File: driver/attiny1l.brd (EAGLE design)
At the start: 160 x 100 mm, 7 parts, among them IC1 ATTiny85, IC2 74AHC1G00DCK, IC3 74AHC1G00DCK, IC4 LB1973M, J1 AVR_SPI_PRG_6NS

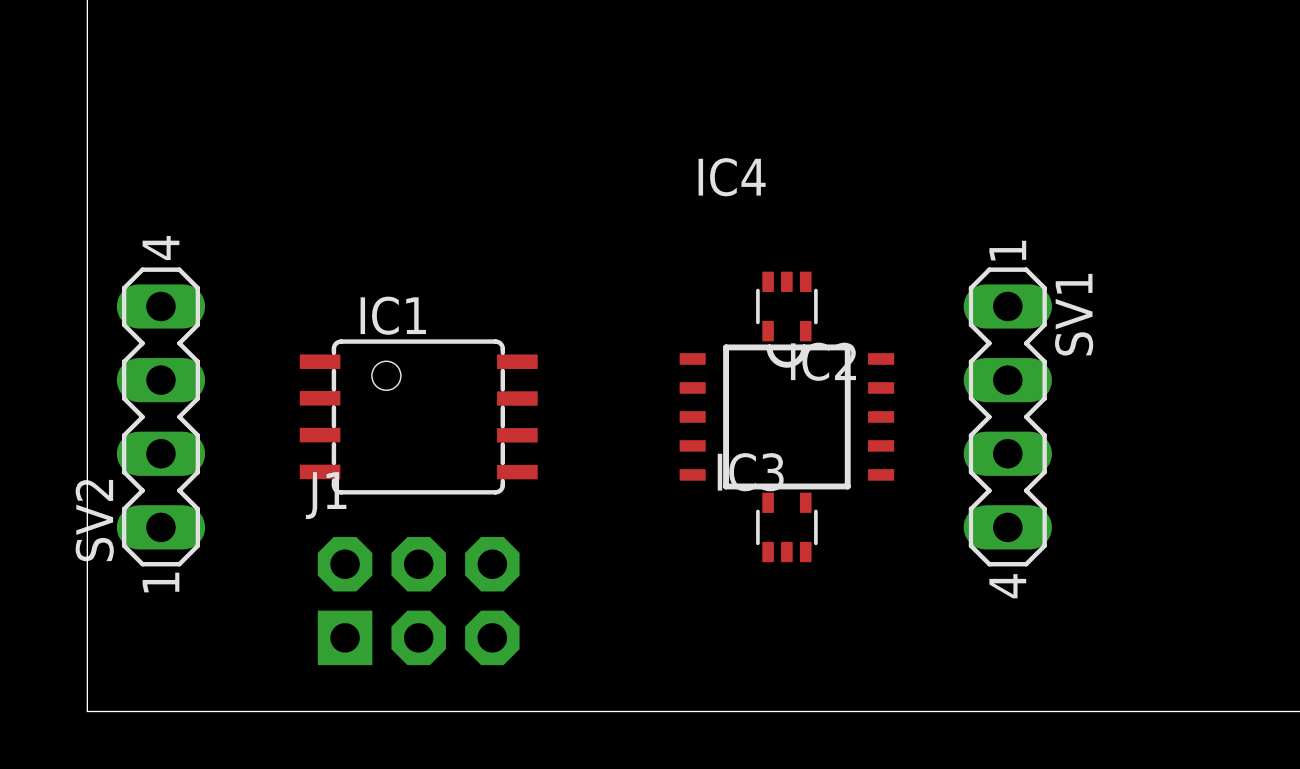
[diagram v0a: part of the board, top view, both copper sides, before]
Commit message: basic autorouter and drc configs for 1-layer board
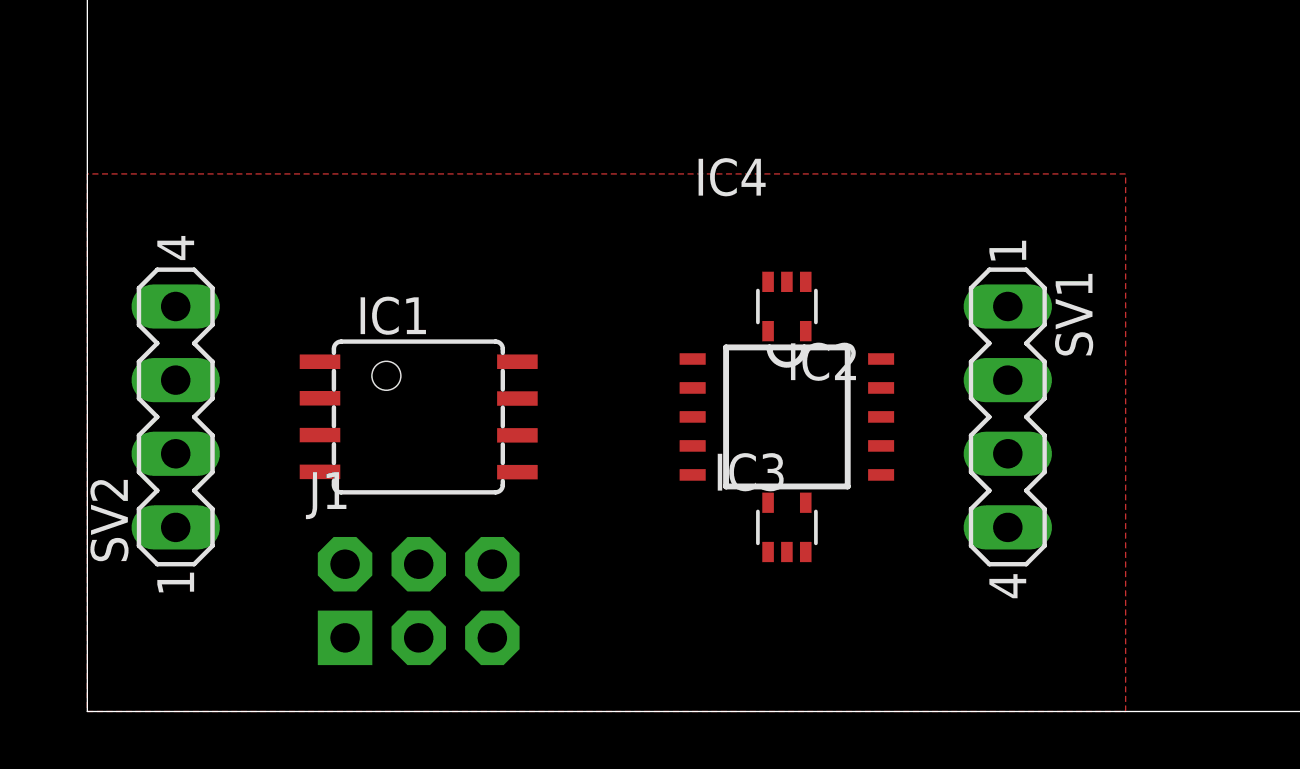
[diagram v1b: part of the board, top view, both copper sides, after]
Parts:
- moved SV2 0.51 mm to (3.05, 10.2)
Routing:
- added copper zone on layer 1, net GND
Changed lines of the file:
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@@
 <layer number="14" name="Route14" color="1" fill="6" visible="no" active="no"/>
 <layer number="15" name="Route15" color="4" fill="6" visible="no" active="no"/>
-<layer number="16" name="Bottom" color="1" fill="1" visible="yes" active="yes"/>
+<layer number="16" name="Bottom" color="1" fill="1" visible="no" active="no"/>
 <layer number="17" name="Pads" color="2" fill="1" visible="yes" active="yes"/>
 <layer number="18" name="Vias" color="2" fill="1" visible="yes" active="yes"/>
@@
 necessary adjustments and save your customized
 design rules under a new name.</description>
-<param name="layerSetup" value="(1*16)"/>
+<param name="layerSetup" value="1"/>
 <param name="mtCopper" value="0.035mm 0.035mm 0.035mm 0.035mm 0.035mm 0.035mm 0.035mm 0.035mm 0.035mm 0.035mm 0.035mm 0.035mm 0.035mm 0.035mm 0.035mm 0.035mm"/>
 <param name="mtIsolate" value="1.5mm 0.15mm 0.2mm 0.15mm 0.2mm 0.15mm 0.2mm 0.15mm 0.2mm 0.15mm 0.2mm 0.15mm 0.2mm 0.15mm 0.2mm"/>
@@
 <param name="mdDrill" value="8mil"/>
 <param name="mdSmdStop" value="0mil"/>
-<param name="msWidth" value="10mil"/>
+<param name="msWidth" value="6mil"/>
 <param name="msDrill" value="24mil"/>
 <param name="msMicroVia" value="9.99mm"/>
@@
 <autorouter>
 <pass name="Default">
-<param name="RoutingGrid" value="50mil"/>
+<param name="RoutingGrid" value="2.5mil"/>
 <param name="tpViaShape" value="round"/>
-<param name="PrefDir.1" value="|"/>
+<param name="PrefDir.1" value="-"/>
 <param name="PrefDir.2" value="0"/>
 <param name="PrefDir.3" value="0"/>
@@
 <param name="PrefDir.14" value="0"/>
 <param name="PrefDir.15" value="0"/>
-<param name="PrefDir.16" value="-"/>
+<param name="PrefDir.16" value="0"/>
 <param name="cfVia" value="8"/>
 <param name="cfNonPref" value="5"/>
@@
 <attribute name="OC_FARNELL" value="unknown" x="-13.97" y="-10.16" size="1.778" layer="27" rot="R270" display="off"/>
 </element>
-<element name="SV2" library="con-lstb" package="MA04-1" value="" x="2.54" y="10.16" rot="R90">
-<attribute name="OC_NEWARK" value="unknown" x="48.26" y="44.45" size="1.778" layer="27" rot="R90" display="off"/>
-<attribute name="MPN" value="" x="48.26" y="44.45" size="1.778" layer="27" rot="R90" display="off"/>
-<attribute name="MF" value="" x="48.26" y="44.45" size="1.778" layer="27" rot="R90" display="off"/>
-<attribute name="OC_FARNELL" value="unknown" x="48.26" y="44.45" size="1.778" layer="27" rot="R90" display="off"/>
+<element name="SV2" library="con-lstb" package="MA04-1" value="" x="3.048" y="10.16" rot="R90">
+<attribute name="OC_NEWARK" value="unknown" x="48.768" y="44.45" size="1.778" layer="27" rot="R90" display="off"/>
+<attribute name="MPN" value="" x="48.768" y="44.45" size="1.778" layer="27" rot="R90" display="off"/>
+<attribute name="MF" value="" x="48.768" y="44.45" size="1.778" layer="27" rot="R90" display="off"/>
+<attribute name="OC_FARNELL" value="unknown" x="48.768" y="44.45" size="1.778" layer="27" rot="R90" display="off"/>
 </element>
 <element name="IC4" library="LB1973M" package="SSOP10" value="LB1973M" x="24.13" y="10.16"/>
@@
 <contactref element="J1" pad="1"/>
 <contactref element="IC4" pad="4"/>
-<wire x1="23.48" y1="5.5" x2="24.13" y2="5.5" width="0" layer="19" extent="1-1"/>
-<wire x1="14.834" y1="9.525" x2="23.48" y2="5.5" width="0" layer="19" extent="1-1"/>
+<wire x1="24.13" y1="5.5" x2="23.48" y2="5.5" width="0" layer="19" extent="1-1"/>
+<wire x1="20.88" y1="9.16" x2="23.48" y2="5.5" width="0" layer="19" extent="1-1"/>
+<wire x1="14.834" y1="9.525" x2="20.88" y2="9.16" width="0" layer="19" extent="1-1"/>
 <wire x1="8.89" y1="2.54" x2="14.834" y2="9.525" width="0" layer="19" extent="1-1"/>
-<wire x1="20.88" y1="9.16" x2="8.89" y2="2.54" width="0" layer="19" extent="1-1"/>
 </signal>
 <signal name="IN3">
@@
 <contactref element="IC4" pad="3"/>
 <wire x1="24.78" y1="14.82" x2="24.13" y2="14.82" width="0" layer="19" extent="1-1"/>
-<wire x1="8.026" y1="9.535" x2="24.78" y2="14.82" width="0" layer="19" extent="1-1"/>
-<wire x1="20.88" y1="10.16" x2="8.026" y2="9.535" width="0" layer="19" extent="1-1"/>
+<wire x1="20.88" y1="10.16" x2="24.13" y2="14.82" width="0" layer="19" extent="1-1"/>
+<wire x1="8.026" y1="9.535" x2="20.88" y2="10.16" width="0" layer="19" extent="1-1"/>
 </signal>
 <signal name="GND">
@@
 <contactref element="IC4" pad="6"/>
 <contactref element="IC4" pad="6"/>
-<wire x1="23.48" y1="14.82" x2="24.78" y2="5.5" width="0" layer="19" extent="1-1"/>
-<wire x1="13.97" y1="5.08" x2="23.48" y2="14.82" width="0" layer="19" extent="1-1"/>
-<wire x1="8.026" y1="8.265" x2="13.97" y2="5.08" width="0" layer="19" extent="1-1"/>
-<wire x1="2.54" y1="13.97" x2="8.026" y2="8.265" width="0" layer="19" extent="1-1"/>
-<wire x1="27.38" y1="8.16" x2="8.026" y2="8.265" width="0" layer="19" extent="1-1"/>
+<polygon width="0.2032" layer="1" isolate="0.2032">
+<vertex x="0" y="18.542"/>
+<vertex x="0" y="0"/>
+<vertex x="35.814" y="0"/>
+<vertex x="35.814" y="18.542"/>
+</polygon>
 </signal>
 <signal name="+5V">
@@
 <contactref element="SV2" pad="1"/>
 <contactref element="IC4" pad="1"/>
-<wire x1="24.78" y1="13.12" x2="23.48" y2="7.2" width="0" layer="19" extent="1-1"/>
-<wire x1="14.834" y1="12.065" x2="24.78" y2="13.12" width="0" layer="19" extent="1-1"/>
+<wire x1="20.88" y1="12.16" x2="24.78" y2="13.12" width="0" layer="19" extent="1-1"/>
+<wire x1="23.48" y1="7.2" x2="20.88" y2="12.16" width="0" layer="19" extent="1-1"/>
+<wire x1="14.834" y1="12.065" x2="20.88" y2="12.16" width="0" layer="19" extent="1-1"/>
 <wire x1="8.89" y1="5.08" x2="14.834" y2="12.065" width="0" layer="19" extent="1-1"/>
-<wire x1="2.54" y1="6.35" x2="8.89" y2="5.08" width="0" layer="19" extent="1-1"/>
-<wire x1="20.88" y1="12.16" x2="2.54" y2="6.35" width="0" layer="19" extent="1-1"/>
+<wire x1="3.048" y1="6.35" x2="8.89" y2="5.08" width="0" layer="19" extent="1-1"/>
 </signal>
 <signal name="SDA/MOSI">
@@
 <contactref element="SV2" pad="3"/>
 <wire x1="11.43" y1="5.08" x2="14.834" y2="8.255" width="0" layer="19" extent="1-1"/>
-<wire x1="2.54" y1="11.43" x2="11.43" y2="5.08" width="0" layer="19" extent="1-1"/>
+<wire x1="3.048" y1="11.43" x2="11.43" y2="5.08" width="0" layer="19" extent="1-1"/>
 </signal>
 <signal name="N$6">
@@
 <contactref element="SV2" pad="2"/>
 <wire x1="11.43" y1="2.54" x2="14.834" y2="10.795" width="0" layer="19" extent="1-1"/>
-<wire x1="2.54" y1="8.89" x2="11.43" y2="2.54" width="0" layer="19" extent="1-1"/>
+<wire x1="3.048" y1="8.89" x2="11.43" y2="2.54" width="0" layer="19" extent="1-1"/>
 </signal>
 <signal name="OUT4">

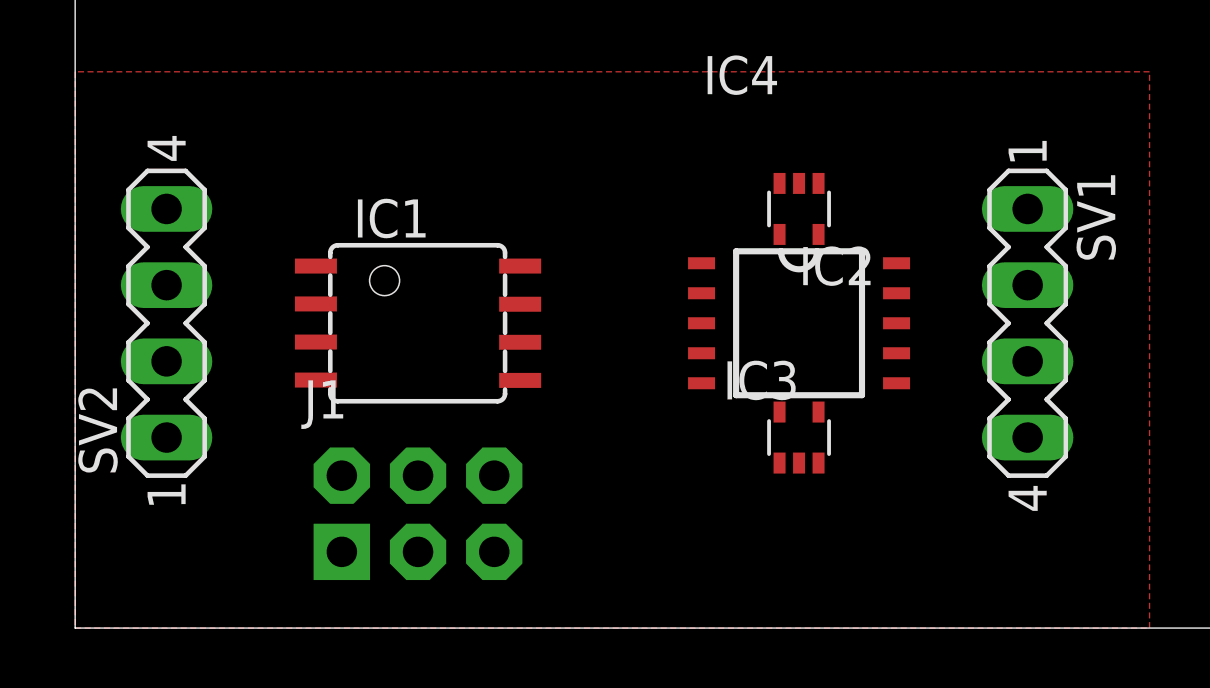
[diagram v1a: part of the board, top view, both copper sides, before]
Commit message: 1L routing done, some airwires will be needed but that is to be expected
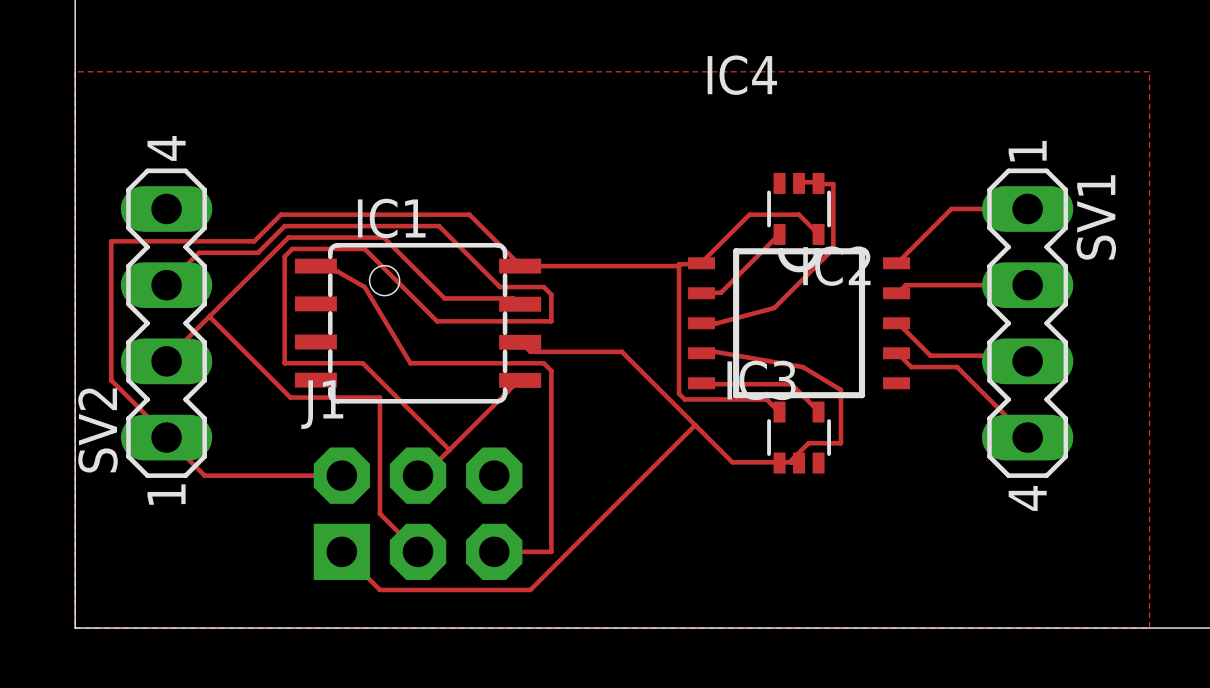
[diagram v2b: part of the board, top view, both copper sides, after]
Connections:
- net IN1 renamed IN1/MISO
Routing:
- net +5V: track 0.00 -> 47.2 mm
- net SDA/MOSI: track 0.00 -> 40.4 mm
- net IN1/MISO: track 0.00 -> 34.2 mm
- net SCL/SCK: track 0.00 -> 26.9 mm
- net N$6: track 0.00 -> 17.5 mm
- net IN3: track 0.00 -> 8.65 mm
- net OUT2: track 0.00 -> 5.53 mm
- net OUT4: track 0.00 -> 5.12 mm
- net OUT1: track 0.00 -> 4.90 mm
- net OUT3: track 0.00 -> 4.48 mm
- net IN2: track 0.00 -> 4.32 mm
- net IN4: track 0.00 -> 3.41 mm

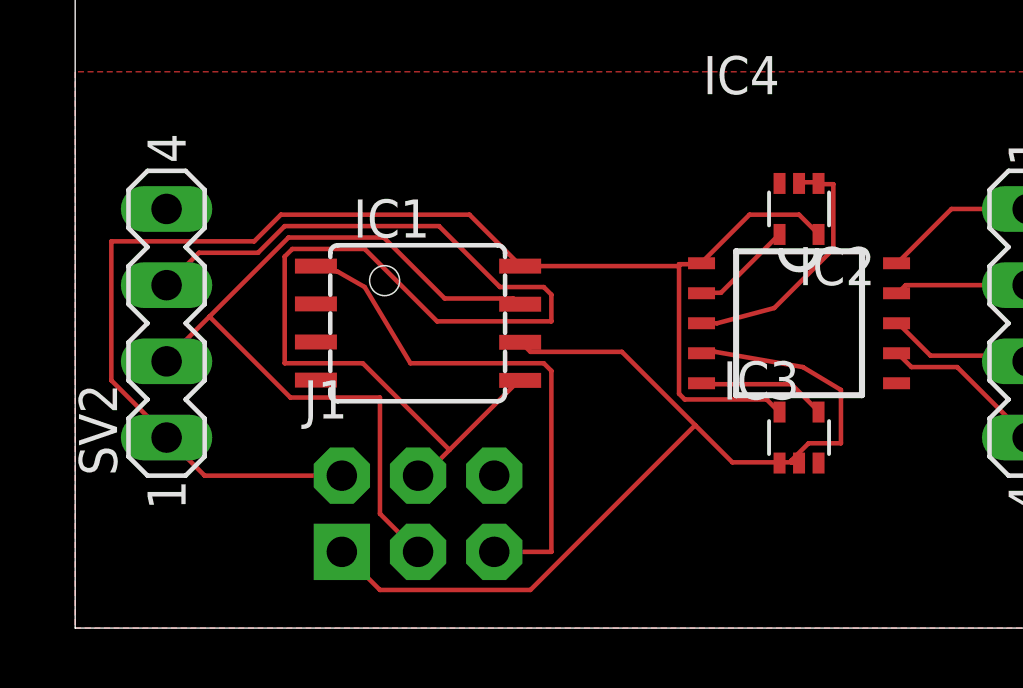
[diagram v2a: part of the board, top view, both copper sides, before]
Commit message: rotating the attiny gave better results
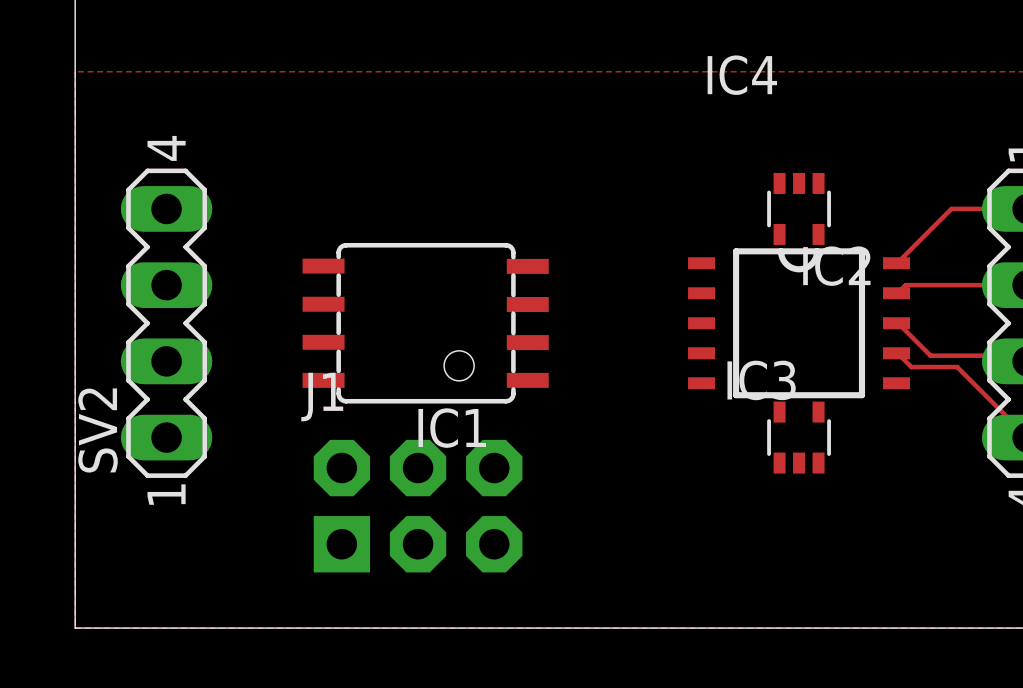
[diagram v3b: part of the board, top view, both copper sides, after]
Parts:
- moved J1 0.25 mm to (11.4, 4.06)
- moved IC1 0.25 mm to (11.7, 10.2), turned to 90 degrees
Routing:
- net +5V: track 47.2 -> 0.00 mm
- net SDA/MOSI: track 40.4 -> 0.00 mm
- net IN1/MISO: track 34.2 -> 0.00 mm
- net SCL/SCK: track 26.9 -> 0.00 mm
- net N$6: track 17.5 -> 0.00 mm
- net IN3: track 8.65 -> 0.00 mm
- net IN2: track 4.32 -> 0.00 mm
- net IN4: track 3.41 -> 0.00 mm

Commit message: I guess I forgot to save...
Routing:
- net IN1/MISO: track 0.00 -> 67.0 mm
- net +5V: track 0.00 -> 36.3 mm
- net SCL/SCK: track 0.00 -> 21.8 mm
- net IN3: track 0.00 -> 14.6 mm
- net SDA/MOSI: track 0.00 -> 14.1 mm
- net N$6: track 0.00 -> 6.81 mm
- net IN4: track 0.00 -> 5.69 mm
- net IN2: track 0.00 -> 4.86 mm

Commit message: adjust dimension
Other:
- board size 160 x 100 mm -> 35.8 x 20 mm
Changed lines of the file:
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@@
 <board>
 <plain>
-<wire x1="0" y1="0" x2="160" y2="0" width="0" layer="20"/>
-<wire x1="160" y1="0" x2="160" y2="100" width="0" layer="20"/>
-<wire x1="160" y1="100" x2="0" y2="100" width="0" layer="20"/>
-<wire x1="0" y1="100" x2="0" y2="0" width="0" layer="20"/>
+<wire x1="0" y1="0" x2="35.794" y2="0" width="0" layer="20"/>
+<wire x1="35.794" y1="0" x2="35.794" y2="19.99" width="0" layer="20"/>
+<wire x1="35.794" y1="19.99" x2="0" y2="19.99" width="0" layer="20"/>
+<wire x1="0" y1="19.99" x2="0" y2="0" width="0" layer="20"/>
 </plain>
 <attributes>

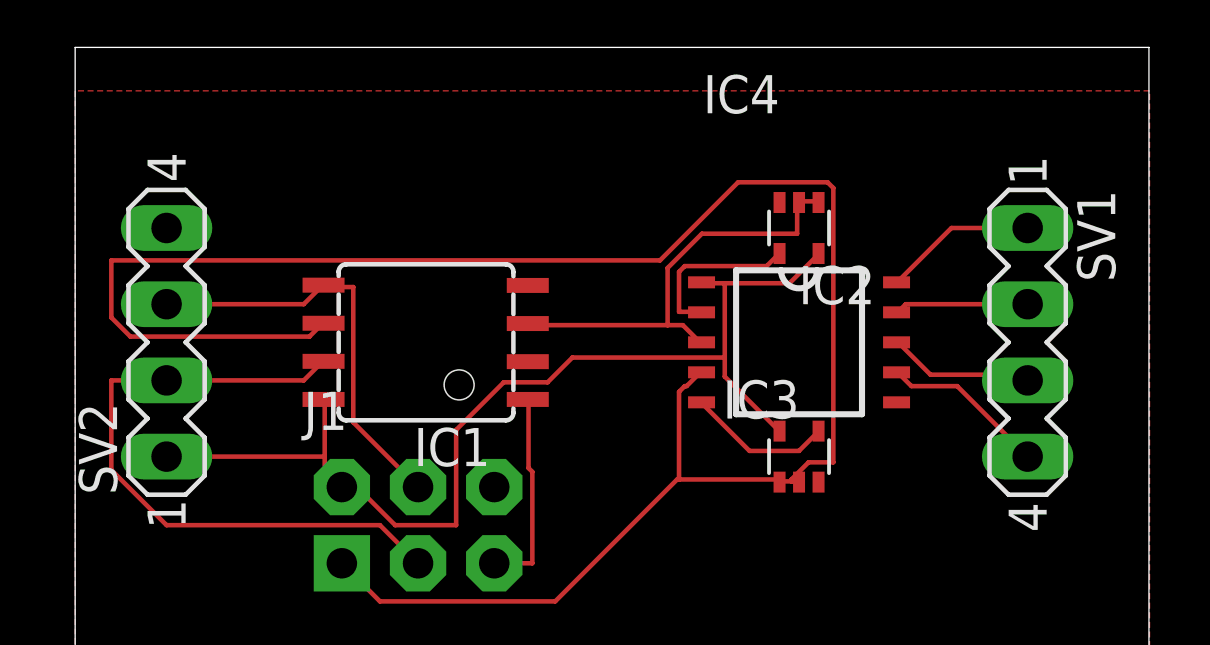
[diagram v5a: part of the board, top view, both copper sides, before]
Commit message: adjust routing for easier soldering withoud soldermask
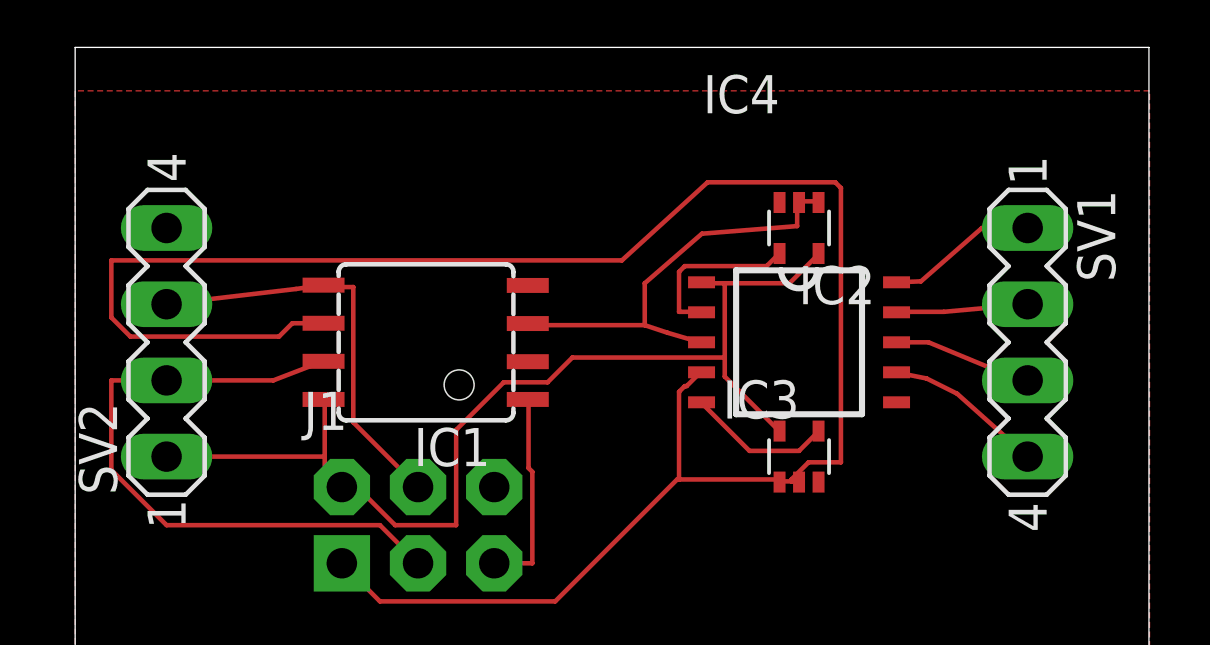
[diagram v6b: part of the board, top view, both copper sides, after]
